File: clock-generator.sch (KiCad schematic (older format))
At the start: 7 parts

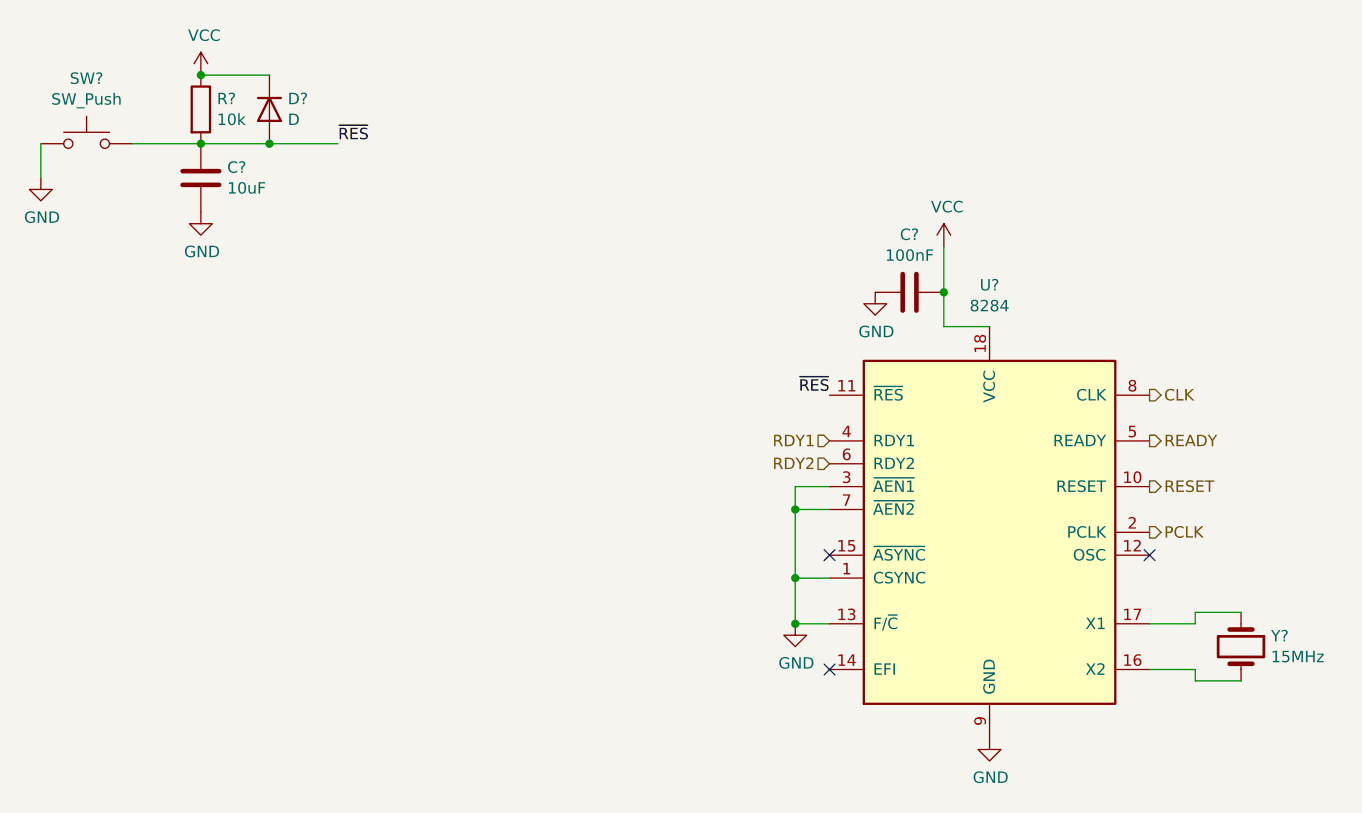
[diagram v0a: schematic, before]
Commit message: created 28F010 CMOS flash block; improved power decoupling; added M/~IO pin from 8086 sheet; reduced no. of logic gates in 8086 processor block; added +12V; moved input power to external-connectors sheet; annotated schematics
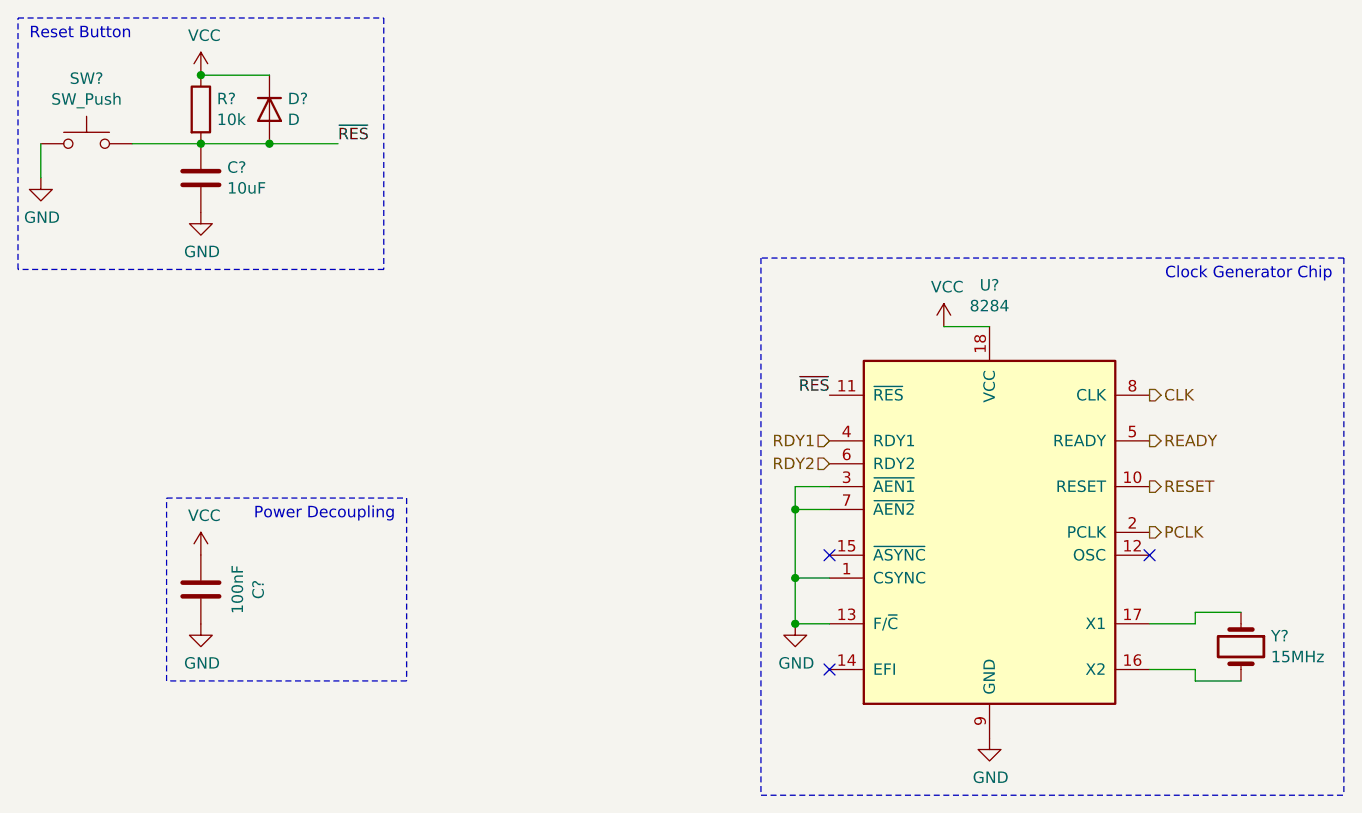
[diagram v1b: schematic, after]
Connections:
- net GND: now also C?.2; no longer C?.1
- net VCC: now also C?.1; no longer C?.2
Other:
- note added: "Clock Generator Chip"
- note added: "Power Decoupling"
- note added: "Reset Button"
- moved on the sheet: C?
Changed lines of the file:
@@
 $Descr A4 11693 8268
 encoding utf-8
-Sheet 4 4
+Sheet 4 5
 Title "clock-generator"
 Date ""
@@
 $EndComp
 $Comp
-L power:VCC #PWR0121
-U 1 1 619336A7
-P 5500 2350
-F 0 "#PWR0121" H 5500 2200 50  0001 C CNN
-F 1 "VCC" H 5515 2523 50  0000 C CNN
-F 2 "" H 5500 2350 50  0001 C CNN
-F 3 "" H 5500 2350 50  0001 C CNN
-	1    5500 2350
-	1    0    0    -1
-$EndComp
-$Comp
 L Device:C C?
 U 1 1 61933DA5
-P 5350 2550
-F 0 "C?" V 5602 2550 50  0000 C CNN
-F 1 "100nF" V 5511 2550 50  0000 C CNN
-F 2 "" H 5388 2400 50  0001 C CNN
-F 3 "~" H 5350 2550 50  0001 C CNN
-	1    5350 2550
-	0    -1   -1   0
+P 2250 3850
+F 0 "C?" V 2502 3850 50  0000 C CNN
+F 1 "100nF" V 2411 3850 50  0000 C CNN
+F 2 "" H 2288 3700 50  0001 C CNN
+F 3 "~" H 2250 3850 50  0001 C CNN
+	1    2250 3850
+	1    0    0    -1
 $EndComp
 Wire Wire Line
 	5700 2700 5500 2700
-Wire Wire Line
-	5500 2700 5500 2550
 $Comp
 L power:GND #PWR0122
 U 1 1 61939686
-P 5200 2550
-F 0 "#PWR0122" H 5200 2300 50  0001 C CNN
-F 1 "GND" H 5205 2377 50  0000 C CNN
-F 2 "" H 5200 2550 50  0001 C CNN
-F 3 "" H 5200 2550 50  0001 C CNN
-	1    5200 2550
+P 2250 4000
+F 0 "#PWR0122" H 2250 3750 50  0001 C CNN
+F 1 "GND" H 2255 3827 50  0000 C CNN
+F 2 "" H 2250 4000 50  0001 C CNN
+F 3 "" H 2250 4000 50  0001 C CNN
+	1    2250 4000
 	1    0    0    -1
 $EndComp
@@
 RDY2
 NoConn ~ 5000 3700
-Connection ~ 5500 2550
-Wire Wire Line
-	5500 2550 5500 2350
 Wire Wire Line
 	5000 3400 4850 3400
@@
 Wire Wire Line
 	4850 3500 4850 3800
+$Comp
+L power:VCC #PWR?
+U 1 1 61C7475F
+P 2250 3700
+F 0 "#PWR?" H 2250 3550 50  0001 C CNN
+F 1 "VCC" H 2265 3873 50  0000 C CNN
+F 2 "" H 2250 3700 50  0001 C CNN
+F 3 "" H 2250 3700 50  0001 C CNN
+	1    2250 3700
+	1    0    0    -1
+$EndComp
+$Comp
+L power:VCC #PWR?
+U 1 1 61C74E11
+P 5500 2700
+F 0 "#PWR?" H 5500 2550 50  0001 C CNN
+F 1 "VCC" H 5515 2873 50  0000 C CNN
+F 2 "" H 5500 2700 50  0001 C CNN
+F 3 "" H 5500 2700 50  0001 C CNN
+	1    5500 2700
+	1    0    0    -1
+$EndComp
+Wire Notes Line
+	7250 2400 4700 2400
+Wire Notes Line
+	4700 2400 4700 4750
+Wire Notes Line
+	4700 4750 7250 4750
+Wire Notes Line
+	7250 2400 7250 4750
+Text Notes 7200 2500 2    50   ~ 0
+Clock Generator Chip
+Text Notes 3100 3550 2    50   ~ 0
+Power Decoupling
+Wire Notes Line
+	3150 3450 3150 4250
+Wire Notes Line
+	3150 4250 2100 4250
+Wire Notes Line
+	2100 4250 2100 3450
+Wire Notes Line
+	2100 3450 3150 3450
+Wire Notes Line
+	1450 2450 1450 1350
+Wire Notes Line
+	1450 1350 3050 1350
+Wire Notes Line
+	3050 1350 3050 2450
+Wire Notes Line
+	3050 2450 1450 2450
+Text Notes 1500 1450 0    50   ~ 0
+Reset Button
 $EndSCHEMATC
